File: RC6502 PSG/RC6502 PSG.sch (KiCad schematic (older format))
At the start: 26 parts, among them J1 Out, J2 Port, J3 Base, J4 RC6502_Backplane, U1 LM386, U2 74LS373, U3 74LS138, U4 74LS138, U5 SN76489AN, X1 TCXO-14

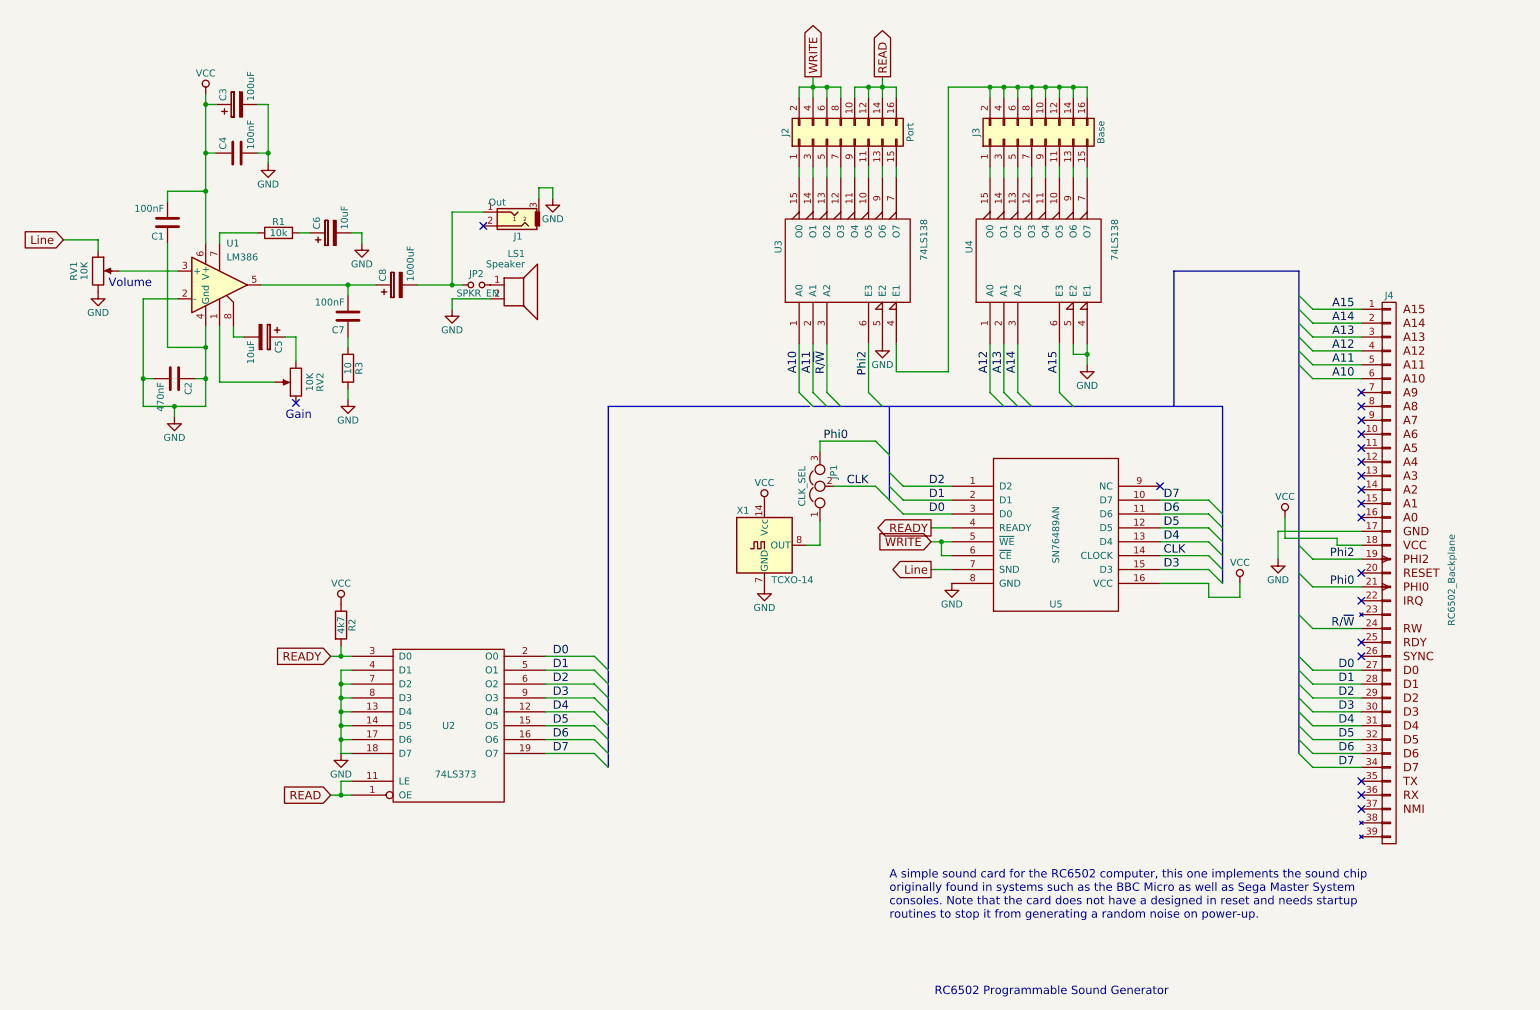
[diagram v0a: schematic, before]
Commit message: PSG sound card layout
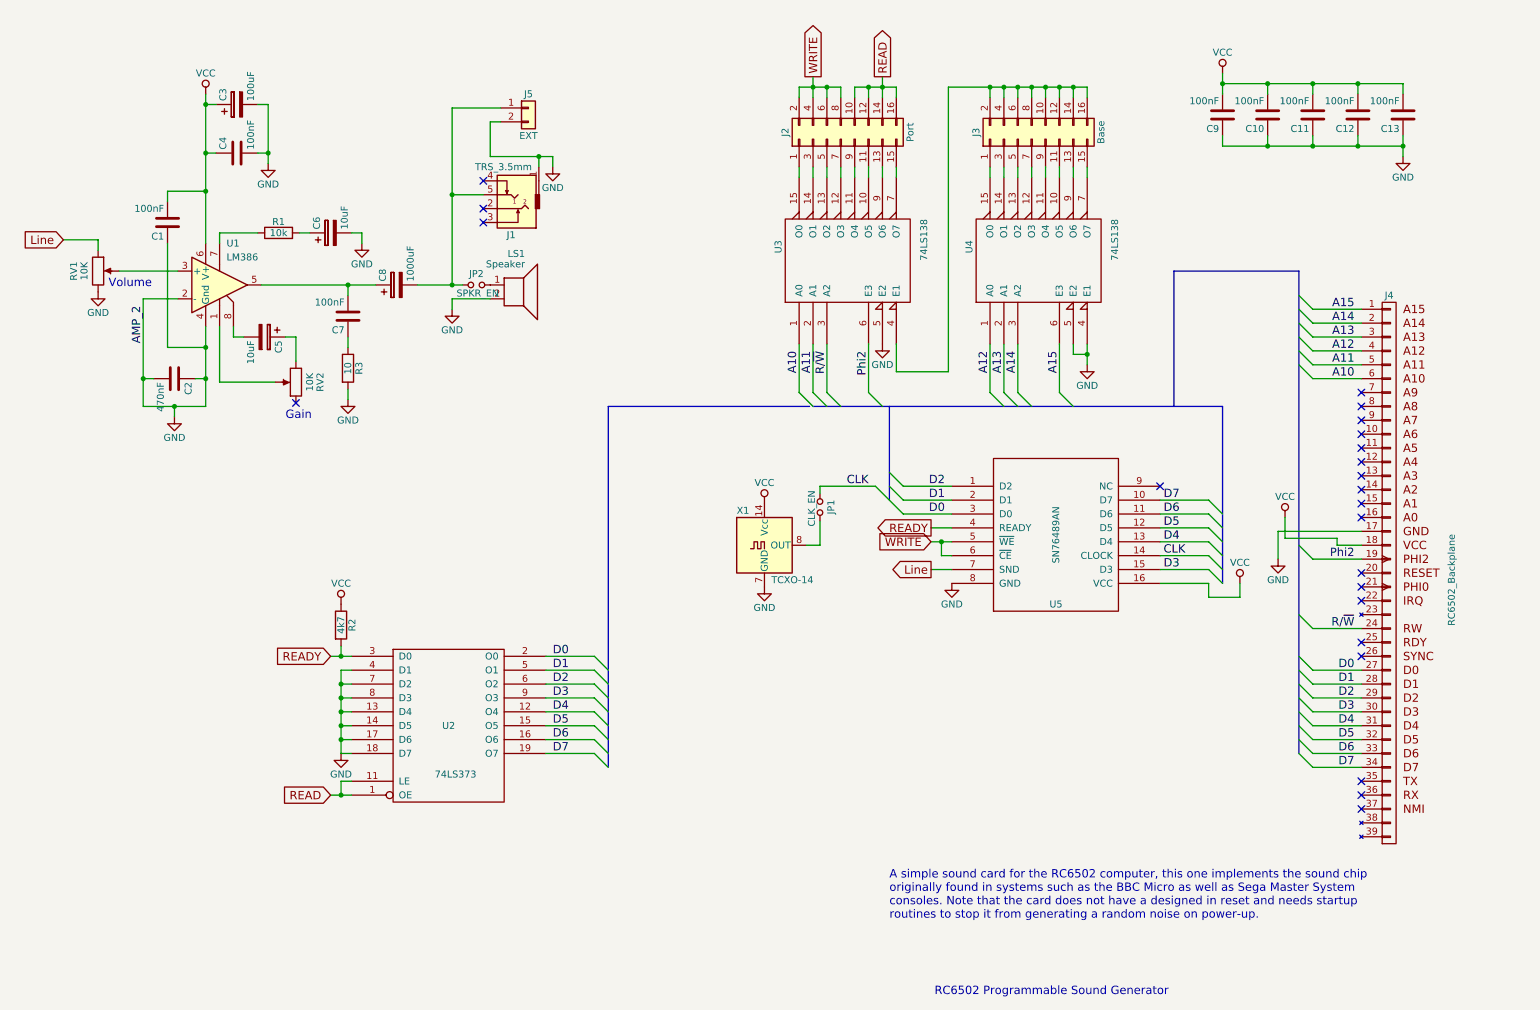
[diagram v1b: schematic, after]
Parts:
- removed J1: Out, Pin_Headers:Pin_Header_Straight_1x03_Pitch2.54mm, symbol Audio-Jack-3
- removed JP1: CLK_SEL, Pin_Headers:Pin_Header_Straight_1x03_Pitch2.54mm, symbol Jumper_NC_Dual
- added C10, C11, C12, C13, C9: 100nF, Capacitors_THT:C_Disc_D4.7mm_W2.5mm_P5.00mm, symbol C
- added J1: TRS_3.5mm, TRS:Tayda_3.5mm_stereo_TRS_jack_A-853, symbol TRS_3.5mm
- added J5: EXT, Pin_Headers:Pin_Header_Angled_1x02_Pitch2.54mm, symbol Conn_01x02
- added JP1: CLK_EN, Pin_Headers:Pin_Header_Straight_1x02_Pitch2.54mm, symbol Jumper_NO_Small
- C3: footprint Capacitors_THT:CP_Radial_D4.0mm_P2.00mm -> Capacitors_THT:CP_Radial_D5.0mm_P2.50mm
- C5, C6: footprint Capacitors_THT:CP_Radial_Tantal_D5.0mm_P5.00mm -> Capacitors_THT:CP_Radial_D5.0mm_P2.50mm
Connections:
- net CLK: now also JP1.1
- net GND: now also C10.1, C11.1, C12.1, C13.1, C9.1, J1.1, J5.2 (Pin_2)
- net VCC: now also C10.2, C11.2, C12.2, C13.2, C9.2
- net at X1.8 (OUT): now also JP1.2
- net at C8.2, JP2.1: now also J1.5, J5.1 (Pin_1)
- net Phi0: no longer names the net of J4.21 (PHI0)
- no-connect marks 20 -> 23
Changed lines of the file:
@@
 LIBS:SN76489AN
 LIBS:Oscillators
+LIBS:trs_3.5mm
 LIBS:RC6502 PSG-cache
 EELAYER 25 0
@@
 	6925 3825 7025 3925
 Wire Wire Line
-	6625 3825 6925 3825
+	6525 3825 6925 3825
 Text Label 9000 4325 0    60   ~ 0
-CLK
-Text Label 6875 3825 2    60   ~ 0
 CLK
 $Comp
@@
 F 0 "C3" H 2350 1175 50  0000 L CNN
 F 1 "100uF" H 2350 975 50  0000 L CNN
-F 2 "Capacitors_THT:CP_Radial_D4.0mm_P2.00mm" H 2363 925 50  0001 C CNN
+F 2 "Capacitors_THT:CP_Radial_D5.0mm_P2.50mm" H 2363 925 50  0001 C CNN
 F 3 "" H 2325 1075 50  0001 C CNN
 	1    2325 1075
@@
 F 0 "C5" H 2550 2850 50  0000 L CNN
 F 1 "10uF" H 2550 2650 50  0000 L CNN
-F 2 "Capacitors_THT:CP_Radial_Tantal_D5.0mm_P5.00mm" H 2563 2600 50  0001 C CNN
+F 2 "Capacitors_THT:CP_Radial_D5.0mm_P2.50mm" H 2563 2600 50  0001 C CNN
 F 3 "" H 2525 2750 50  0001 C CNN
 	1    2525 2750
@@
 F 0 "C6" H 3025 2100 50  0000 L CNN
 F 1 "10uF" H 3025 1900 50  0000 L CNN
-F 2 "Capacitors_THT:CP_Radial_Tantal_D5.0mm_P5.00mm" H 3038 1850 50  0001 C CNN
+F 2 "Capacitors_THT:CP_Radial_D5.0mm_P2.50mm" H 3038 1850 50  0001 C CNN
 F 3 "" H 3000 2000 50  0001 C CNN
 	1    3000 2000
@@
 Line
 $Comp
-L Audio-Jack-3 J1
-U 1 1 5C233E8D
-P 4300 1850
-F 0 "J1" H 4250 2025 50  0000 C CNN
-F 1 "Out" H 4400 1780 50  0000 C CNN
-F 2 "Pin_Headers:Pin_Header_Straight_1x03_Pitch2.54mm" H 4550 1950 50  0001 C CNN
-F 3 "" H 4550 1950 50  0001 C CNN
-	1    4300 1850
-	-1   0    0    1
-$EndComp
-$Comp
 L GND #PWR013
 U 1 1 5C234708
-P 4600 1750
-F 0 "#PWR013" H 4600 1500 50  0001 C CNN
-F 1 "GND" H 4600 1600 50  0000 C CNN
-F 2 "" H 4600 1750 50  0001 C CNN
-F 3 "" H 4600 1750 50  0001 C CNN
-	1    4600 1750
+P 4600 1525
+F 0 "#PWR013" H 4600 1275 50  0001 C CNN
+F 1 "GND" H 4600 1375 50  0000 C CNN
+F 2 "" H 4600 1525 50  0001 C CNN
+F 3 "" H 4600 1525 50  0001 C CNN
+	1    4600 1525
 	1    0    0    -1
 $EndComp
@@
 	1    0    0    -1
 $EndComp
-$Comp
-L Jumper_NC_Dual JP1
-U 1 1 5C235BBC
-P 6525 3825
-F 0 "JP1" H 6575 3725 50  0000 L CNN
-F 1 "CLK_SEL" H 6525 3925 50  0000 C BNN
-F 2 "Pin_Headers:Pin_Header_Straight_1x03_Pitch2.54mm" H 6525 3825 50  0001 C CNN
-F 3 "" H 6525 3825 50  0001 C CNN
-	1    6525 3825
-	0    -1   -1   0
-$EndComp
 Wire Wire Line
 	6425 4250 6525 4250
 Wire Wire Line
 	6525 4250 6525 4075
-Text Label 10375 4550 2    60   ~ 0
-Phi0
-Wire Wire Line
-	10425 4550 10075 4550
-Entry Wire Line
-	9975 4450 10075 4550
-Text Label 6550 3500 0    60   ~ 0
-Phi0
-Entry Wire Line
-	6925 3500 7025 3600
-Wire Wire Line
-	6525 3500 6925 3500
-Wire Wire Line
-	6525 3500 6525 3575
 $Comp
 L R R2
@@
 $EndComp
 Wire Wire Line
-	3875 1850 4100 1850
+	3875 1725 4100 1725
 Connection ~ 3875 2375
 Wire Wire Line
-	4500 1750 4500 1675
-Wire Wire Line
-	4500 1675 4600 1675
-Wire Wire Line
-	4600 1675 4600 1750
-Wire Wire Line
-	3875 2375 3875 1850
-NoConn ~ 4100 1950
+	4500 1525 4500 1450
+Wire Wire Line
+	4150 1450 4600 1450
+Wire Wire Line
+	4600 1450 4600 1525
+Wire Wire Line
+	3875 1100 3875 2375
+NoConn ~ 4100 1825
 $Comp
 L GND #PWR017
@@
 Text Notes 7025 6950 0    60   ~ 0
 A simple sound card for the RC6502 computer, this one implements the sound chip\noriginally found in systems such as the BBC Micro as well as Sega Master System\nconsoles. Note that the card does not have a designed in reset and needs startup\nroutines to stop it from generating a random noise on power-up.
+NoConn ~ 4100 1625
+NoConn ~ 4100 1925
+$Comp
+L TRS_3.5mm J1
+U 1 1 5C2450A7
+P 4300 1725
+F 0 "J1" H 4300 2015 50  0000 C CNN
+F 1 "TRS_3.5mm" H 4150 1525 50  0000 L CNN
+F 2 "TRS:Tayda_3.5mm_stereo_TRS_jack_A-853" H 4550 1825 50  0001 C CNN
+F 3 "" H 4550 1825 50  0001 C CNN
+	1    4300 1725
+	-1   0    0    1
+$EndComp
+$Comp
+L C C9
+U 1 1 5C245DE4
+P 9425 1150
+F 0 "C9" H 9450 1250 50  0000 L CNN
+F 1 "100nF" H 9450 1050 50  0000 L CNN
+F 2 "Capacitors_THT:C_Disc_D4.7mm_W2.5mm_P5.00mm" H 9463 1000 50  0001 C CNN
+F 3 "" H 9425 1150 50  0001 C CNN
+	1    9425 1150
+	-1   0    0    1
+$EndComp
+$Comp
+L C C10
+U 1 1 5C24602B
+P 9750 1150
+F 0 "C10" H 9775 1250 50  0000 L CNN
+F 1 "100nF" H 9775 1050 50  0000 L CNN
+F 2 "Capacitors_THT:C_Disc_D4.7mm_W2.5mm_P5.00mm" H 9788 1000 50  0001 C CNN
+F 3 "" H 9750 1150 50  0001 C CNN
+	1    9750 1150
+	-1   0    0    1
+$EndComp
+$Comp
+L C C11
+U 1 1 5C24609D
+P 10075 1150
+F 0 "C11" H 10100 1250 50  0000 L CNN
+F 1 "100nF" H 10100 1050 50  0000 L CNN
+F 2 "Capacitors_THT:C_Disc_D4.7mm_W2.5mm_P5.00mm" H 10113 1000 50  0001 C CNN
+F 3 "" H 10075 1150 50  0001 C CNN
+	1    10075 1150
+	-1   0    0    1
+$EndComp
+Wire Wire Line
+	9425 850  9425 1000
+Wire Wire Line
+	9425 925  10725 925
+Wire Wire Line
+	10075 925  10075 1000
+Wire Wire Line
+	9750 1000 9750 925
+Connection ~ 9750 925
+Wire Wire Line
+	9425 1300 9425 1375
+Wire Wire Line
+	9425 1375 10725 1375
+Wire Wire Line
+	10075 1375 10075 1300
+Wire Wire Line
+	9750 1300 9750 1375
+Connection ~ 9750 1375
+$Comp
+L C C12
+U 1 1 5C2637FC
+P 10400 1150
+F 0 "C12" H 10425 1250 50  0000 L CNN
+F 1 "100nF" H 10425 1050 50  0000 L CNN
+F 2 "Capacitors_THT:C_Disc_D4.7mm_W2.5mm_P5.00mm" H 10438 1000 50  0001 C CNN
+F 3 "" H 10400 1150 50  0001 C CNN
+	1    10400 1150
+	-1   0    0    1
+$EndComp
+$Comp
+L C C13
+U 1 1 5C26387E
+P 10725 1150
+F 0 "C13" H 10750 1250 50  0000 L CNN
+F 1 "100nF" H 10750 1050 50  0000 L CNN
+F 2 "Capacitors_THT:C_Disc_D4.7mm_W2.5mm_P5.00mm" H 10763 1000 50  0001 C CNN
+F 3 "" H 10725 1150 50  0001 C CNN
+	1    10725 1150
+	-1   0    0    1
+$EndComp
+Wire Wire Line
+	10725 925  10725 1000
+Connection ~ 10075 925
+Wire Wire Line
+	10725 1300 10725 1450
+Connection ~ 10075 1375
+Wire Wire Line
+	10400 1300 10400 1375
+Connection ~ 10400 1375
+Wire Wire Line
+	10400 1000 10400 925
+Connection ~ 10400 925
+$Comp
+L GND #PWR019
+U 1 1 5C263DDE
+P 10725 1450
+F 0 "#PWR019" H 10725 1200 50  0001 C CNN
+F 1 "GND" H 10725 1300 50  0000 C CNN
+F 2 "" H 10725 1450 50  0001 C CNN
+F 3 "" H 10725 1450 50  0001 C CNN
+	1    10725 1450
+	1    0    0    -1
+$EndComp
+Connection ~ 10725 1375
+$Comp
+L VCC #PWR020
+U 1 1 5C264246
+P 9425 850
+F 0 "#PWR020" H 9425 700 50  0001 C CNN
+F 1 "VCC" H 9425 1000 50  0000 C CNN
+F 2 "" H 9425 850 50  0001 C CNN
+F 3 "" H 9425 850 50  0001 C CNN
+	1    9425 850
+	1    0    0    -1
+$EndComp
+Connection ~ 9425 925
+$Comp
+L Jumper_NO_Small JP1
+U 1 1 5C265B84
+P 6525 3975
+F 0 "JP1" H 6525 4055 50  0000 C CNN
+F 1 "CLK_EN" H 6535 3915 50  0000 C CNN
+F 2 "Pin_Headers:Pin_Header_Straight_1x02_Pitch2.54mm" H 6525 3975 50  0001 C CNN
+F 3 "" H 6525 3975 50  0001 C CNN
+	1    6525 3975
+	0    1    1    0
+$EndComp
+Wire Wire Line
+	6525 3875 6525 3825
+NoConn ~ 10425 4550
+Text Label 6875 3825 2    60   ~ 0
+CLK
+$Comp
+L Conn_01x02 J5
+U 1 1 5C266EC8
+P 4425 1100
+F 0 "J5" H 4425 1200 50  0000 C CNN
+F 1 "EXT" H 4425 900 50  0000 C CNN
+F 2 "Pin_Headers:Pin_Header_Angled_1x02_Pitch2.54mm" H 4425 1100 50  0001 C CNN
+F 3 "" H 4425 1100 50  0001 C CNN
+	1    4425 1100
+	1    0    0    -1
+$EndComp
+Wire Wire Line
+	4150 1450 4150 1200
+Wire Wire Line
+	4150 1200 4225 1200
+Connection ~ 4500 1450
+Wire Wire Line
+	3875 1100 4225 1100
+Connection ~ 3875 1725
+Text Label 1650 2525 3    60   ~ 0
+AMP_2
 $EndSCHEMATC

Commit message: Revised PSG module
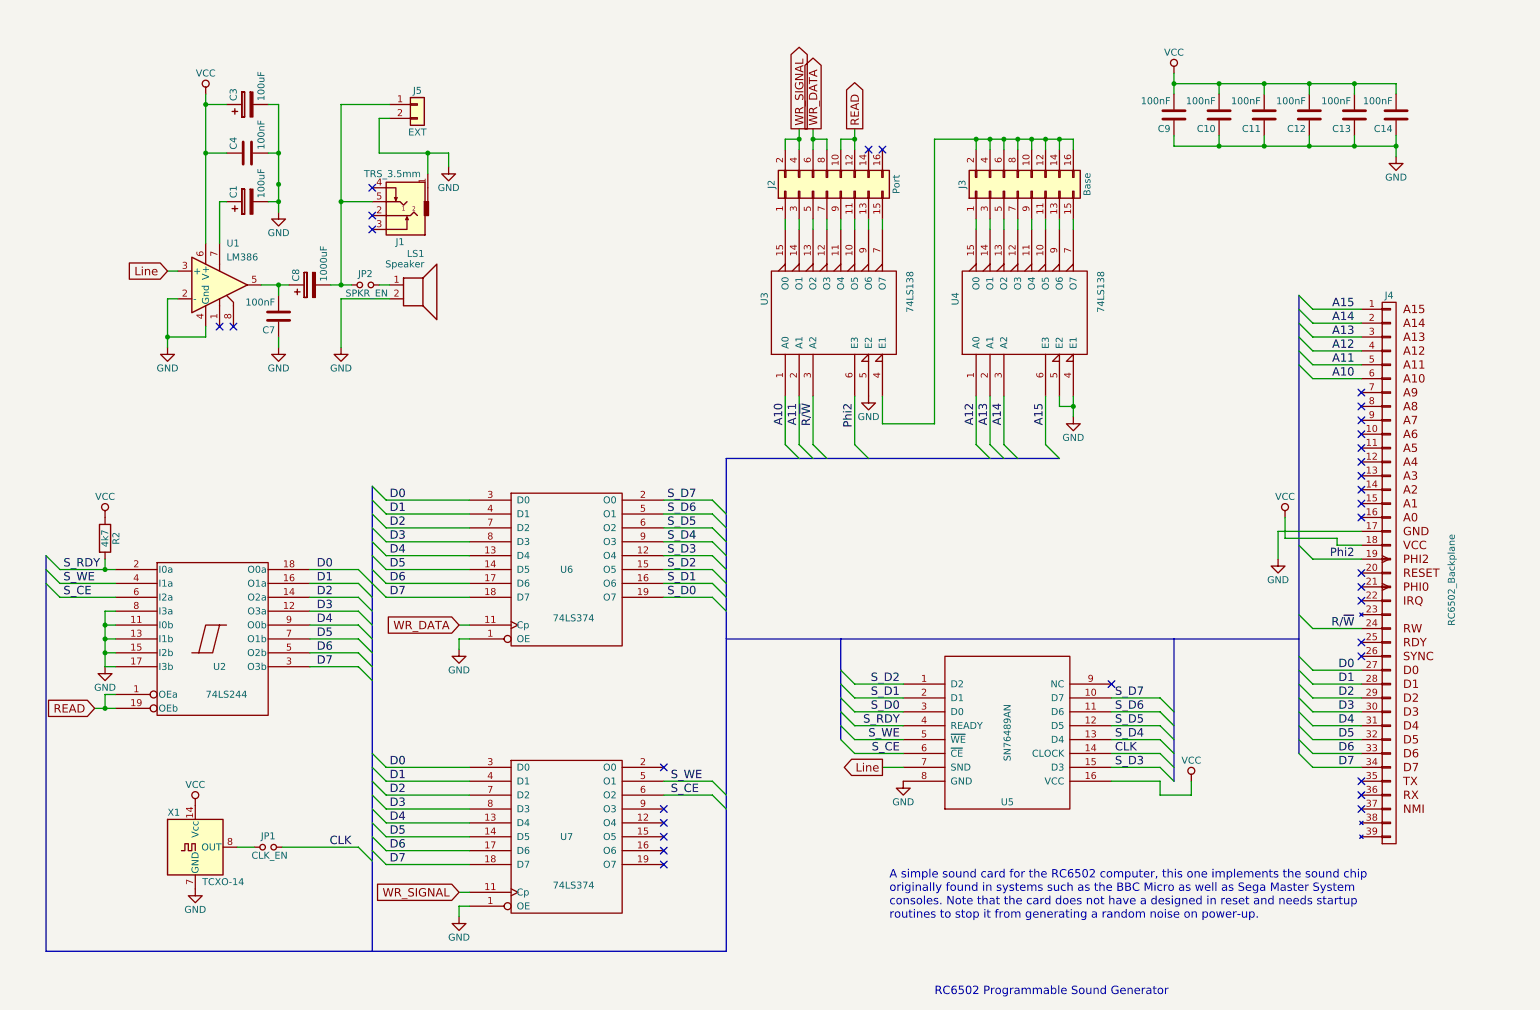
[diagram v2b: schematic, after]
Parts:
- removed C1: 100nF, Capacitors_THT:C_Disc_D4.7mm_W2.5mm_P5.00mm, symbol C
- removed C2: 470nF, Capacitors_THT:C_Disc_D4.7mm_W2.5mm_P5.00mm, symbol C
- removed C5, C6: 10uF, Capacitors_THT:CP_Radial_D5.0mm_P2.50mm, symbol CP
- removed R1: 10k, Resistors_THT:R_Axial_DIN0207_L6.3mm_D2.5mm_P10.16mm_Horizontal, symbol R
- removed R3: 10, Resistors_THT:R_Axial_DIN0207_L6.3mm_D2.5mm_P10.16mm_Horizontal, symbol R
- removed RV1, RV2: 10K, Potentiometers:Potentiometer_Trimmer_Bourns_3296W, symbol POT
- removed U2: 74LS373, Housings_DIP:DIP-20_W7.62mm, symbol 74LS373
- added C1: 100uF, Capacitors_THT:CP_Radial_D5.0mm_P2.50mm, symbol CP
- added C14: 100nF, Capacitors_THT:C_Disc_D4.7mm_W2.5mm_P5.00mm, symbol C
- added U2: 74LS244, Housings_DIP:DIP-20_W7.62mm_Socket, symbol 74LS244
- added U6, U7: 74LS374, Housings_DIP:DIP-20_W7.62mm_Socket, symbol 74LS374
- U3, U4: footprint Housings_DIP:DIP-16_W7.62mm -> Housings_DIP:DIP-16_W7.62mm_Socket
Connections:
- net CLK: now also JP1.2; no longer JP1.1
- net D0: now also U2.18 (O0a), U6.3 (D0), U7.3 (D0); no longer U5.3 (D0)
- net D1: now also U2.16 (O1a), U6.4 (D1), U7.4 (D1); no longer U5.2 (D1)
- net D2: now also U2.14 (O2a), U6.7 (D2), U7.7 (D2); no longer U5.1 (D2)
- net D3: now also U2.12 (O3a), U6.8 (D3), U7.8 (D3); no longer U5.15 (D3)
- net D4: now also U2.9 (O0b), U6.13 (D4), U7.13 (D4); no longer U5.13 (D4)
- net D5: now also U2.7 (O1b), U6.14 (D5), U7.14 (D5); no longer U5.12 (D5)
- net D6: now also U2.5 (O2b), U6.17 (D6), U7.17 (D6); no longer U5.11 (D6)
- net D7: now also U2.3 (O3b), U6.18 (D7), U7.18 (D7); no longer U5.10 (D7)
- net GND: now also C7.1, C1.2, C14.1, U2.10 (GND), U2.11 (I0b), U2.13 (I1b), U2.15 (I2b), U2.17 (I3b), U2.8 (I3a), U6.1 (OE), U6.10 (GND), U7.1 (OE), U7.10 (GND)
- net Line: now also U1.3 (+)
- net READ: now also U2.1 (OEa), U2.19 (OEb); no longer J2.14 (Pin_14), J2.16 (Pin_16)
- net VCC: now also C14.2, U2.20 (VCC), U6.20 (VCC), U7.20 (VCC)
- net at X1.8 (OUT): now also JP1.1; no longer JP1.2
- net at U1.7: now also C1.1
- net READY renamed S_RDY
- net S_RDY: now also U2.2 (I0a)
- removed net WRITE: J2.2 (Pin_2), J2.4 (Pin_4), J2.6 (Pin_6), J2.8 (Pin_8), U5.5 (~WE), U5.6 (~CE)
- new net S_CE: U2.6 (I2a), U5.6 (~CE), U7.6 (O2)
- new net S_D0: U5.3 (D0), U6.19 (O7)
- new net S_D1: U5.2 (D1), U6.16 (O6)
- new net S_D2: U5.1 (D2), U6.15 (O5)
- new net S_D3: U5.15 (D3), U6.12 (O4)
- new net S_D4: U5.13 (D4), U6.9 (O3)
- new net S_D5: U5.12 (D5), U6.6 (O2)
- new net S_D6: U5.11 (D6), U6.5 (O1)
- new net S_D7: U5.10 (D7), U6.2 (O0)
- new net S_WE: U2.4 (I1a), U5.5 (~WE), U7.5 (O1)
- new net WR_DATA: J2.6 (Pin_6), J2.8 (Pin_8), U6.11 (Cp)
- new net WR_SIGNAL: J2.2 (Pin_2), J2.4 (Pin_4), U7.11 (Cp)
- no-connect marks 23 -> 32
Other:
- note removed: "Gain"
- note removed: "Volume"
- moved on the sheet: C10, C11, C12, C13, C3, C4, C7, C8, C9, J1, J2, J3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
